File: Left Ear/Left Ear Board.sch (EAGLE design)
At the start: 23 parts

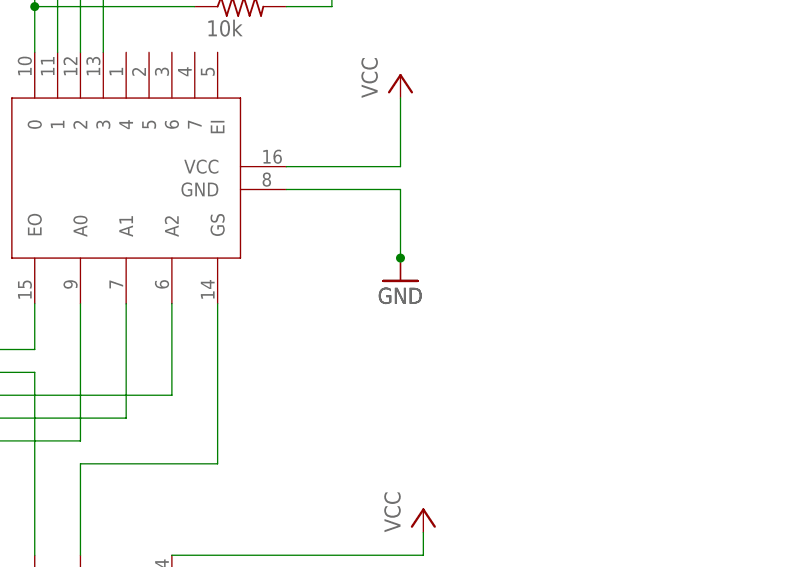
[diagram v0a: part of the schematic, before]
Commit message: Made changes
Change LED caps to .1uF on right ear and center
Add resistor to D2
Add level shifters (1 for D1, 1 for D2)
Add mount holes on right ear
Add mosfet for servo (see things to consider.txt)
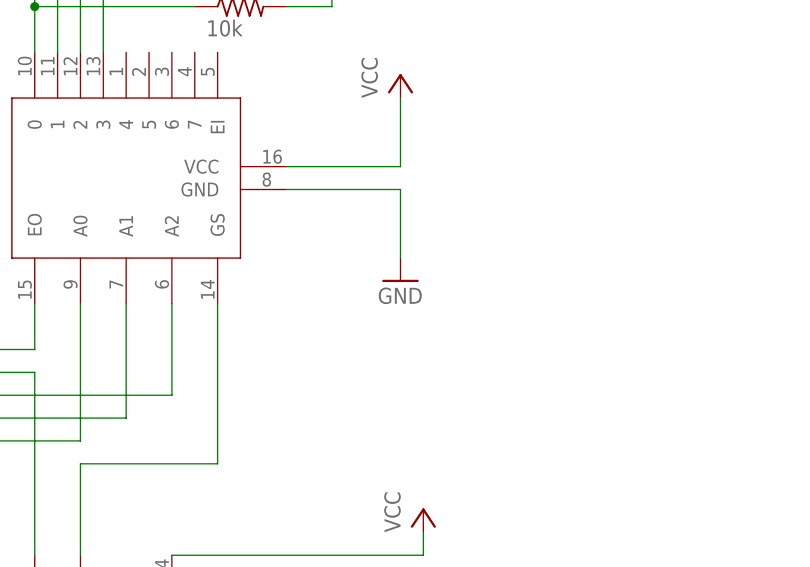
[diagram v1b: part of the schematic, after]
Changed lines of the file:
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@@
 <?xml version="1.0" encoding="utf-8"?>
 <!DOCTYPE eagle SYSTEM "eagle.dtd">
-<eagle version="8.5.0">
+<eagle version="8.3.1">
 <drawing>
 <settings>
@@
 <part name="U$3" library="FormE" deviceset="SN74LS148D" device=""/>
 <part name="P+2" library="supply1" library_urn="urn:adsk.eagle:library:371" deviceset="VCC" device=""/>
-<part name="GND2" library="supply1" library_urn="urn:adsk.eagle:library:371" deviceset="GND" device=""/>
 <part name="U$1" library="FormE" deviceset="12-POSITION-ROTARY" device=""/>
 <part name="GND3" library="supply1" library_urn="urn:adsk.eagle:library:371" deviceset="GND" device=""/>
@@
 <instance part="U$3" gate="G$1" x="198.12" y="40.64"/>
 <instance part="P+2" gate="VCC" x="187.96" y="55.88"/>
-<instance part="GND2" gate="1" x="187.96" y="33.02"/>
 <instance part="U$1" gate="G$1" x="137.16" y="83.82" rot="R270"/>
 <instance part="GND3" gate="1" x="187.96" y="33.02"/>
@@
 <segment>
 <pinref part="U$3" gate="G$1" pin="GND"/>
-<pinref part="GND2" gate="1" pin="GND"/>
 <wire x1="175.26" y1="43.18" x2="187.96" y2="43.18" width="0.1524" layer="91"/>
 <wire x1="187.96" y1="43.18" x2="187.96" y2="35.56" width="0.1524" layer="91"/>
 <pinref part="GND3" gate="1" pin="GND"/>
-<junction x="187.96" y="35.56"/>
-</segment>
-<segment>
+</segment>
+<segment>

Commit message: Worked on code
Updated board layouts since shit changed
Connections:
- net GND: no longer JP3.2, JP4.2, JP5.2, JP6.2
- net N$21: now also JP3.2; no longer JP3.1
- net N$22: now also JP4.2; no longer JP4.1
- net N$23: now also JP5.2; no longer JP5.1
- net N$24: now also JP6.2; no longer JP6.1
- net VCC: now also JP3.1, JP4.1, JP5.1, JP6.1
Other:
- moved on the sheet: JP3, JP4, JP5, JP6
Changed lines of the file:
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@@
 <?xml version="1.0" encoding="utf-8"?>
 <!DOCTYPE eagle SYSTEM "eagle.dtd">
-<eagle version="8.3.1">
+<eagle version="8.6.1">
 <drawing>
 <settings>
@@
 <part name="JP5" library="pinhead" library_urn="urn:adsk.eagle:library:325" deviceset="PINHD-1X2" device="" package3d_urn="urn:adsk.eagle:package:22435/2"/>
 <part name="JP6" library="pinhead" library_urn="urn:adsk.eagle:library:325" deviceset="PINHD-1X2" device="" package3d_urn="urn:adsk.eagle:package:22435/2"/>
-<part name="GND7" library="supply1" library_urn="urn:adsk.eagle:library:371" deviceset="GND" device=""/>
 <part name="R1" library="rcl" deviceset="R-US_" device="R0603" value="10k">
 <attribute name="PARTNO" value="ERJ-3EKF2201V"/>
@@
 <part name="P+5" library="supply1" library_urn="urn:adsk.eagle:library:371" deviceset="VCC" device=""/>
 <part name="P+6" library="supply1" library_urn="urn:adsk.eagle:library:371" deviceset="VCC" device=""/>
+<part name="P+7" library="supply1" library_urn="urn:adsk.eagle:library:371" deviceset="VCC" device=""/>
 </parts>
 <sheets>
@@
 <instance part="GND6" gate="1" x="198.12" y="-63.5"/>
 <instance part="JP7" gate="A" x="203.2" y="-96.52" rot="R180"/>
-<instance part="JP3" gate="G$1" x="243.84" y="-116.84"/>
-<instance part="JP4" gate="G$1" x="261.62" y="-116.84"/>
-<instance part="JP5" gate="G$1" x="279.4" y="-116.84"/>
-<instance part="JP6" gate="G$1" x="294.64" y="-116.84"/>
-<instance part="GND7" gate="1" x="228.6" y="-132.08"/>
+<instance part="JP3" gate="G$1" x="241.3" y="-86.36"/>
+<instance part="JP4" gate="G$1" x="259.08" y="-86.36"/>
+<instance part="JP5" gate="G$1" x="276.86" y="-86.36"/>
+<instance part="JP6" gate="G$1" x="292.1" y="-86.36"/>
 <instance part="R1" gate="G$1" x="78.74" y="60.96">
 <attribute name="PARTNO" x="78.74" y="60.96" size="1.778" layer="96" rot="R90" display="off"/>
@@
 <instance part="P+5" gate="VCC" x="68.58" y="119.38"/>
 <instance part="P+6" gate="VCC" x="180.34" y="91.44"/>
+<instance part="P+7" gate="VCC" x="228.6" y="-73.66"/>
 </instances>
 <busses>
@@
 <junction x="68.58" y="68.58"/>
 </segment>
+<segment>
+<pinref part="JP3" gate="G$1" pin="1"/>
+<wire x1="238.76" y1="-83.82" x2="228.6" y2="-83.82" width="0.1524" layer="91"/>
+<pinref part="P+7" gate="VCC" pin="VCC"/>
+<wire x1="228.6" y1="-83.82" x2="228.6" y2="-78.74" width="0.1524" layer="91"/>
+<pinref part="JP4" gate="G$1" pin="1"/>
+<wire x1="228.6" y1="-78.74" x2="228.6" y2="-76.2" width="0.1524" layer="91"/>
+<wire x1="256.54" y1="-83.82" x2="251.46" y2="-83.82" width="0.1524" layer="91"/>
+<wire x1="251.46" y1="-83.82" x2="251.46" y2="-78.74" width="0.1524" layer="91"/>
+<wire x1="251.46" y1="-78.74" x2="228.6" y2="-78.74" width="0.1524" layer="91"/>
+<junction x="228.6" y="-78.74"/>
+<pinref part="JP5" gate="G$1" pin="1"/>
+<wire x1="274.32" y1="-83.82" x2="269.24" y2="-83.82" width="0.1524" layer="91"/>
+<wire x1="269.24" y1="-83.82" x2="269.24" y2="-78.74" width="0.1524" layer="91"/>
+<wire x1="269.24" y1="-78.74" x2="251.46" y2="-78.74" width="0.1524" layer="91"/>
+<junction x="251.46" y="-78.74"/>
+<pinref part="JP6" gate="G$1" pin="1"/>
+<wire x1="289.56" y1="-83.82" x2="284.48" y2="-83.82" width="0.1524" layer="91"/>
+<wire x1="284.48" y1="-83.82" x2="284.48" y2="-78.74" width="0.1524" layer="91"/>
+<wire x1="284.48" y1="-78.74" x2="269.24" y2="-78.74" width="0.1524" layer="91"/>
+<junction x="269.24" y="-78.74"/>
+</segment>
 </net>
 <net name="GND" class="0">
@@
 <wire x1="205.74" y1="-58.42" x2="198.12" y2="-58.42" width="0.1524" layer="91"/>
 <wire x1="198.12" y1="-58.42" x2="198.12" y2="-60.96" width="0.1524" layer="91"/>
-</segment>
-<segment>
-<pinref part="JP3" gate="G$1" pin="2"/>
-<wire x1="241.3" y1="-116.84" x2="228.6" y2="-116.84" width="0.1524" layer="91"/>
-<wire x1="228.6" y1="-116.84" x2="228.6" y2="-129.54" width="0.1524" layer="91"/>
-<pinref part="GND7" gate="1" pin="GND"/>
-<pinref part="JP4" gate="G$1" pin="2"/>
-<wire x1="259.08" y1="-116.84" x2="248.92" y2="-116.84" width="0.1524" layer="91"/>
-<wire x1="248.92" y1="-116.84" x2="248.92" y2="-129.54" width="0.1524" layer="91"/>
-<wire x1="248.92" y1="-129.54" x2="228.6" y2="-129.54" width="0.1524" layer="91"/>
-<junction x="228.6" y="-129.54"/>
-<pinref part="JP5" gate="G$1" pin="2"/>
-<wire x1="276.86" y1="-116.84" x2="266.7" y2="-116.84" width="0.1524" layer="91"/>
-<wire x1="266.7" y1="-116.84" x2="266.7" y2="-129.54" width="0.1524" layer="91"/>
-<wire x1="266.7" y1="-129.54" x2="248.92" y2="-129.54" width="0.1524" layer="91"/>
-<junction x="248.92" y="-129.54"/>
-<pinref part="JP6" gate="G$1" pin="2"/>
-<wire x1="292.1" y1="-116.84" x2="284.48" y2="-116.84" width="0.1524" layer="91"/>
-<wire x1="284.48" y1="-116.84" x2="284.48" y2="-129.54" width="0.1524" layer="91"/>
-<wire x1="284.48" y1="-129.54" x2="266.7" y2="-129.54" width="0.1524" layer="91"/>
-<junction x="266.7" y="-129.54"/>
 </segment>
 </net>
@@
 <net name="N$21" class="0">
 <segment>
-<pinref part="JP3" gate="G$1" pin="1"/>
-<wire x1="241.3" y1="-114.3" x2="228.6" y2="-114.3" width="0.1524" layer="91"/>
-<wire x1="228.6" y1="-114.3" x2="228.6" y2="-101.6" width="0.1524" layer="91"/>
 <pinref part="JP7" gate="A" pin="1"/>
 <wire x1="228.6" y1="-101.6" x2="205.74" y2="-101.6" width="0.1524" layer="91"/>
+<pinref part="JP3" gate="G$1" pin="2"/>
+<wire x1="238.76" y1="-86.36" x2="228.6" y2="-86.36" width="0.1524" layer="91"/>
+<wire x1="228.6" y1="-86.36" x2="228.6" y2="-101.6" width="0.1524" layer="91"/>
 </segment>
 </net>
@@
 <pinref part="JP7" gate="A" pin="2"/>
 <wire x1="205.74" y1="-99.06" x2="251.46" y2="-99.06" width="0.1524" layer="91"/>
-<wire x1="251.46" y1="-99.06" x2="251.46" y2="-114.3" width="0.1524" layer="91"/>
-<pinref part="JP4" gate="G$1" pin="1"/>
-<wire x1="251.46" y1="-114.3" x2="259.08" y2="-114.3" width="0.1524" layer="91"/>
+<pinref part="JP4" gate="G$1" pin="2"/>
+<wire x1="251.46" y1="-99.06" x2="251.46" y2="-86.36" width="0.1524" layer="91"/>
+<wire x1="251.46" y1="-86.36" x2="256.54" y2="-86.36" width="0.1524" layer="91"/>
 </segment>
 </net>
@@
 <pinref part="JP7" gate="A" pin="3"/>
 <wire x1="205.74" y1="-96.52" x2="269.24" y2="-96.52" width="0.1524" layer="91"/>
-<wire x1="269.24" y1="-96.52" x2="269.24" y2="-114.3" width="0.1524" layer="91"/>
-<pinref part="JP5" gate="G$1" pin="1"/>
-<wire x1="269.24" y1="-114.3" x2="276.86" y2="-114.3" width="0.1524" layer="91"/>
+<pinref part="JP5" gate="G$1" pin="2"/>
+<wire x1="269.24" y1="-96.52" x2="269.24" y2="-86.36" width="0.1524" layer="91"/>
+<wire x1="269.24" y1="-86.36" x2="274.32" y2="-86.36" width="0.1524" layer="91"/>
 </segment>
 </net>
@@
 <pinref part="JP7" gate="A" pin="4"/>
 <wire x1="205.74" y1="-93.98" x2="284.48" y2="-93.98" width="0.1524" layer="91"/>
-<wire x1="284.48" y1="-93.98" x2="284.48" y2="-114.3" width="0.1524" layer="91"/>
-<pinref part="JP6" gate="G$1" pin="1"/>
-<wire x1="284.48" y1="-114.3" x2="292.1" y2="-114.3" width="0.1524" layer="91"/>
-</segment>
-</net>
+<pinref part="JP6" gate="G$1" pin="2"/>
+<wire x1="284.48" y1="-93.98" x2="284.48" y2="-86.36" width="0.1524" layer="91"/>
+<wire x1="284.48" y1="-86.36" x2="289.56" y2="-86.36" width="0.1524" layer="91"/>
+</segment>
+</net>

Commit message: Fix
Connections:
- net GND: now also U$3.EI
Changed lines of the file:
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@@
 <?xml version="1.0" encoding="utf-8"?>
 <!DOCTYPE eagle SYSTEM "eagle.dtd">
-<eagle version="8.6.1">
+<eagle version="8.6.3">
 <drawing>
 <settings>
@@
 <segment>
 <pinref part="U$3" gate="G$1" pin="GND"/>
-<wire x1="175.26" y1="43.18" x2="187.96" y2="43.18" width="0.1524" layer="91"/>
+<wire x1="175.26" y1="43.18" x2="180.34" y2="43.18" width="0.1524" layer="91"/>
+<wire x1="180.34" y1="43.18" x2="187.96" y2="43.18" width="0.1524" layer="91"/>
 <wire x1="187.96" y1="43.18" x2="187.96" y2="35.56" width="0.1524" layer="91"/>
 <pinref part="GND3" gate="1" pin="GND"/>
-</segment>
-<segment>
+<pinref part="U$3" gate="G$1" pin="EI"/>
+<wire x1="167.64" y1="58.42" x2="180.34" y2="58.42" width="0.1524" layer="91"/>
+<wire x1="180.34" y1="58.42" x2="180.34" y2="43.18" width="0.1524" layer="91"/>
+<junction x="180.34" y="43.18"/>
+</segment>
+<segment>
